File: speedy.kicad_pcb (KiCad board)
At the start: 2 copper layers, 159.2 x 100 mm, 249 parts, among them IC1 TC4424EPA, IC4 SP721, IC5 LTV827, IC7 TC4424EPA, IC8 TC4424EPA, J1 Conn_02x21_Counter_Clockwise, J2 CONN_01X26, J4 CONN_01X05, Q1 STP62NS04Z, Q10 BC547(b), Q2 STP62NS04Z, Q3 STP62NS04Z, Q4 STP62NS04Z, Q5 STP62NS04Z, Q6 STP62NS04Z, Q7 STP62NS04Z, Q8 STP62NS04Z, Q9 VP3203N3-G, U1 LD1085V50

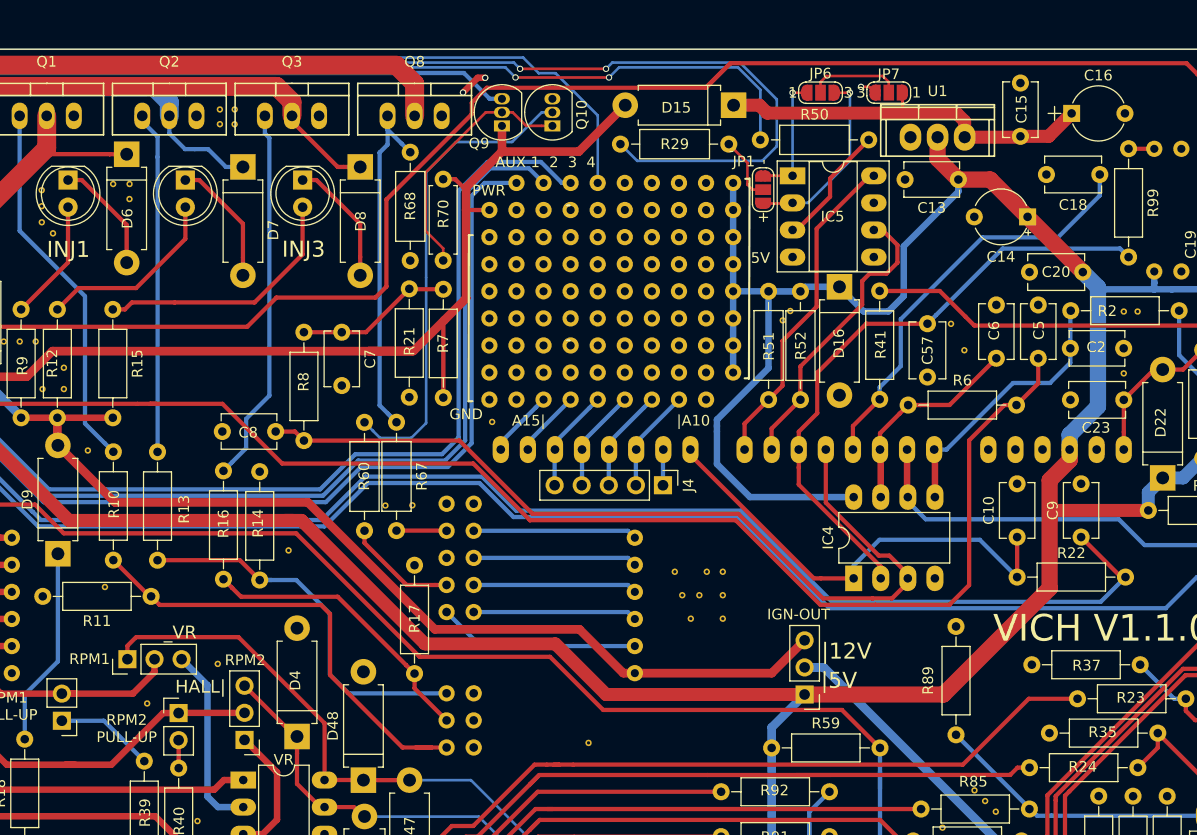
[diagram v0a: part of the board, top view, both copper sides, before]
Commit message: change vreg
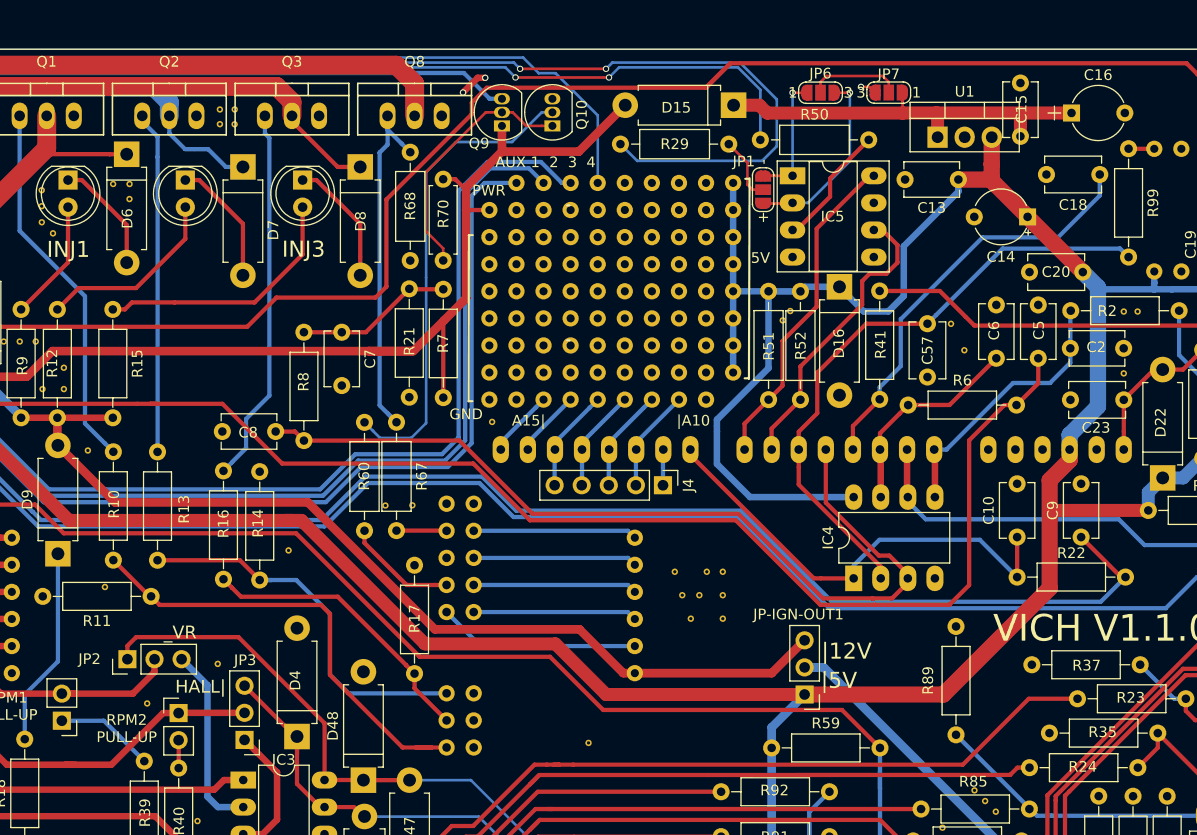
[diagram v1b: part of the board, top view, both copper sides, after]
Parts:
- U1: value LD1085V50 -> L4940-5V; footprint conTE42:TO-220-LongPads -> Package_TO_SOT_THT:TO-220-3_Vertical
- renumbered VR to IC3, IGN-OUT to JP-IGN-OUT1, RPM1 to JP2, RPM2 to JP3, RPM1_PULLUP to JP4, RPM2_PULLUP to JP5
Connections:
- U1 pad 1: GND -> 12V
- U1 pad 2: 5V -> GND
- U1 pad 3: 12V -> 5V
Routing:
- net 12V: track 36.7 -> 38.7 mm
- net 5V: track 448.8 -> 448.1 mm
